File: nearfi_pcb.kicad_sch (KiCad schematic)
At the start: 45 parts, among them J1 PWR_CNN, J2 PROG_CNN, Q1 MMBT3904, SW1 SRST_BTN, U2 TLV1117-33, U3 AT24CS02-STUM, U4 TPL5010, U5 ESP32-S3-MINI-1

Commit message: finished rev D
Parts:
- D1, D4: LCSC C2976072 -> C965555
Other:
- note added: "C5 and C6 should be tantalum capacitors"
- note removed: "Note: - C5 and C6 should be tantalum capacitors"
- moved on the sheet: D8, D9
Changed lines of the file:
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@@
     (stroke (width 0) (type default) (color 0 0 0 0))
   )
-  (wire (pts (xy 173.99 100.33) (xy 173.99 101.6))
+  (wire (pts (xy 173.99 97.79) (xy 173.99 99.06))
     (stroke (width 0) (type default) (color 0 0 0 0))
   )
@@
     (stroke (width 0) (type default) (color 0 0 0 0))
   )
+  (wire (pts (xy 173.99 85.09) (xy 173.99 90.17))
+    (stroke (width 0) (type default) (color 0 0 0 0))
+  )
   (polyline (pts (xy 13.97 121.92) (xy 13.97 161.29))
     (stroke (width 0) (type default) (color 0 0 0 0))
@@
     (stroke (width 0) (type default) (color 0 0 0 0))
   )
-  (wire (pts (xy 167.64 82.55) (xy 167.64 86.36))
-    (stroke (width 0) (type default) (color 0 0 0 0))
-  )
   (wire (pts (xy 20.32 149.86) (xy 20.32 151.13))
     (stroke (width 0) (type default) (color 0 0 0 0))
@@
     (stroke (width 0) (type default) (color 0 0 0 0))
   )
-  (wire (pts (xy 167.64 93.98) (xy 167.64 95.25))
+  (wire (pts (xy 167.64 97.79) (xy 167.64 99.06))
     (stroke (width 0) (type default) (color 0 0 0 0))
   )
@@
     (stroke (width 0) (type dash) (color 0 0 0 0))
   )
+  (wire (pts (xy 167.64 82.55) (xy 167.64 90.17))
+    (stroke (width 0) (type default) (color 0 0 0 0))
+  )
   (wire (pts (xy 152.4 138.43) (xy 152.4 139.7))
     (stroke (width 0) (type default) (color 0 0 0 0))
@@
   )
   (wire (pts (xy 151.13 90.17) (xy 162.56 90.17))
-    (stroke (width 0) (type default) (color 0 0 0 0))
-  )
-  (wire (pts (xy 173.99 85.09) (xy 173.99 92.71))
     (stroke (width 0) (type default) (color 0 0 0 0))
   )
@@
     (effects (font (size 2 2)) (justify left bottom))
   )
-  (text "Note: \n- C5 and C6 should be tantalum capacitors" (at 194.31 62.23 0)
+  (text "C5 and C6 should be\ntantalum capacitors" (at 200.66 59.69 0)
     (effects (font (size 1.27 1.27)) (justify left bottom))
   )
@@
     (pin "1")
   )
-  (symbol (lib_id "power:GND") (at 167.64 95.25 0) (unit 1)
-    (in_bom yes) (on_board yes)
-    (property "Reference" "#PWR0130" (id 0) (at 167.64 101.6 0)
-      (effects (font (size 1.27 1.27)) hide)
-    )
-    (property "Value" "GND" (id 1) (at 167.64 99.06 0))
-    (property "Footprint" "" (id 2) (at 167.64 95.25 0)
-      (effects (font (size 1.27 1.27)) hide)
-    )
-    (property "Datasheet" "" (id 3) (at 167.64 95.25 0)
+  (symbol (lib_id "power:GND") (at 167.64 99.06 0) (unit 1)
+    (in_bom yes) (on_board yes)
+    (property "Reference" "#PWR0130" (id 0) (at 167.64 105.41 0)
+      (effects (font (size 1.27 1.27)) hide)
+    )
+    (property "Value" "GND" (id 1) (at 167.64 102.87 0))
+    (property "Footprint" "" (id 2) (at 167.64 99.06 0)
+      (effects (font (size 1.27 1.27)) hide)
+    )
+    (property "Datasheet" "" (id 3) (at 167.64 99.06 0)
       (effects (font (size 1.27 1.27)) hide)
     )
@@
     (pin "1")
   )
-  (symbol (lib_id "Diode:ESD9B5.0ST5G") (at 167.64 90.17 270) (unit 1)
-    (in_bom yes) (on_board yes)
-    (property "Reference" "D8" (id 0) (at 170.18 88.8999 90)
-      (effects (font (size 1.27 1.27)) (justify left))
-    )
-    (property "Value" "ESD9B5.0ST5G" (id 1) (at 170.18 91.44 90)
-      (effects (font (size 1.27 1.27)) (justify left))
-    )
-    (property "Footprint" "Diode_SMD:D_SOD-923" (id 2) (at 167.64 90.17 0)
-      (effects (font (size 1.27 1.27)) hide)
-    )
-    (property "Datasheet" "https://www.onsemi.com/pub/Collateral/ESD9B-D.PDF" (id 3) (at 167.64 90.17 0)
-      (effects (font (size 1.27 1.27)) hide)
-    )
-    (property "Check" "y" (id 4) (at 167.64 90.17 0)
-      (effects (font (size 1.27 1.27)) hide)
-    )
-    (property "LCSC" "C111566" (id 5) (at 167.64 90.17 0)
+  (symbol (lib_id "Diode:ESD9B5.0ST5G") (at 167.64 93.98 90) (mirror x) (unit 1)
+    (in_bom yes) (on_board yes)
+    (property "Reference" "D8" (id 0) (at 165.1 92.7099 90)
+      (effects (font (size 1.27 1.27)) (justify left))
+    )
+    (property "Value" "ESD9B5.0ST5G" (id 1) (at 165.1 95.25 90)
+      (effects (font (size 1.27 1.27)) (justify left))
+    )
+    (property "Footprint" "Diode_SMD:D_SOD-923" (id 2) (at 167.64 93.98 0)
+      (effects (font (size 1.27 1.27)) hide)
+    )
+    (property "Datasheet" "https://www.onsemi.com/pub/Collateral/ESD9B-D.PDF" (id 3) (at 167.64 93.98 0)
+      (effects (font (size 1.27 1.27)) hide)
+    )
+    (property "Check" "y" (id 4) (at 167.64 93.98 0)
+      (effects (font (size 1.27 1.27)) hide)
+    )
+    (property "LCSC" "C111566" (id 5) (at 167.64 93.98 0)
       (effects (font (size 1.27 1.27)) hide)
     )
@@
     (pin "1")
   )
-  (symbol (lib_id "Diode:ESD9B5.0ST5G") (at 173.99 96.52 90) (unit 1)
-    (in_bom yes) (on_board yes)
-    (property "Reference" "D9" (id 0) (at 176.53 95.2499 90)
+  (symbol (lib_id "Diode:ESD9B5.0ST5G") (at 173.99 93.98 90) (unit 1)
+    (in_bom yes) (on_board yes)
+    (property "Reference" "D9" (id 0) (at 176.53 92.7099 90)
       (effects (font (size 1.27 1.27)) (justify right))
     )
-    (property "Value" "ESD9B5.0ST5G" (id 1) (at 176.53 97.79 90)
+    (property "Value" "ESD9B5.0ST5G" (id 1) (at 176.53 95.25 90)
       (effects (font (size 1.27 1.27)) (justify right))
     )
-    (property "Footprint" "Diode_SMD:D_SOD-923" (id 2) (at 173.99 96.52 0)
-      (effects (font (size 1.27 1.27)) hide)
-    )
-    (property "Datasheet" "https://www.onsemi.com/pub/Collateral/ESD9B-D.PDF" (id 3) (at 173.99 96.52 0)
-      (effects (font (size 1.27 1.27)) hide)
-    )
-    (property "Check" "y" (id 4) (at 173.99 96.52 0)
-      (effects (font (size 1.27 1.27)) hide)
-    )
-    (property "LCSC" "C111566" (id 5) (at 173.99 96.52 0)
+    (property "Footprint" "Diode_SMD:D_SOD-923" (id 2) (at 173.99 93.98 0)
+      (effects (font (size 1.27 1.27)) hide)
+    )
+    (property "Datasheet" "https://www.onsemi.com/pub/Collateral/ESD9B-D.PDF" (id 3) (at 173.99 93.98 0)
+      (effects (font (size 1.27 1.27)) hide)
+    )
+    (property "Check" "y" (id 4) (at 173.99 93.98 0)
+      (effects (font (size 1.27 1.27)) hide)
+    )
+    (property "LCSC" "C111566" (id 5) (at 173.99 93.98 0)
       (effects (font (size 1.27 1.27)) hide)
     )
@@
     (pin "2")
   )
-  (symbol (lib_id "power:GND") (at 173.99 101.6 0) (unit 1)
-    (in_bom yes) (on_board yes)
-    (property "Reference" "#PWR0129" (id 0) (at 173.99 107.95 0)
-      (effects (font (size 1.27 1.27)) hide)
-    )
-    (property "Value" "GND" (id 1) (at 173.99 105.41 0))
-    (property "Footprint" "" (id 2) (at 173.99 101.6 0)
-      (effects (font (size 1.27 1.27)) hide)
-    )
-    (property "Datasheet" "" (id 3) (at 173.99 101.6 0)
+  (symbol (lib_id "power:GND") (at 173.99 99.06 0) (unit 1)
+    (in_bom yes) (on_board yes)
+    (property "Reference" "#PWR0129" (id 0) (at 173.99 105.41 0)
+      (effects (font (size 1.27 1.27)) hide)
+    )
+    (property "Value" "GND" (id 1) (at 173.99 102.87 0))
+    (property "Footprint" "" (id 2) (at 173.99 99.06 0)
+      (effects (font (size 1.27 1.27)) hide)
+    )
+    (property "Datasheet" "" (id 3) (at 173.99 99.06 0)
       (effects (font (size 1.27 1.27)) hide)
     )
@@
       (effects (font (size 1.27 1.27)) (justify left top) hide)
     )
-    (property "Datasheet" "https://www.mouser.com/pdfDocs/WS2812B-2020_V10_EN_181106150240761.pdf" (id 3) (at 267.97 48.895 0)
+    (property "Datasheet" "https://datasheet.lcsc.com/lcsc/2012110135_Worldsemi-WS2812B-2020_C965555.pdf" (id 3) (at 267.97 48.895 0)
       (effects (font (size 1.27 1.27)) (justify left top) hide)
     )
-    (property "LCSC" "C2976072" (id 4) (at 265.43 39.37 0)
+    (property "LCSC" "C965555" (id 4) (at 265.43 39.37 0)
       (effects (font (size 1.27 1.27)) hide)
     )
@@
       (effects (font (size 1.27 1.27)) (justify left top) hide)
     )
-    (property "Datasheet" "https://www.mouser.com/pdfDocs/WS2812B-2020_V10_EN_181106150240761.pdf" (id 3) (at 267.97 81.915 0)
+    (property "Datasheet" "https://datasheet.lcsc.com/lcsc/2012110135_Worldsemi-WS2812B-2020_C965555.pdf" (id 3) (at 267.97 81.915 0)
       (effects (font (size 1.27 1.27)) (justify left top) hide)
     )
-    (property "LCSC" "C2976072" (id 4) (at 265.43 72.39 0)
-      (effects (font (size 1.27 1.27)) hide)
-    )
+    (property "LCSC" "C965555" (id 4) (at 265.43 72.39 0)
+      (effects (font (size 1.27 1.27)) hide)
+    )

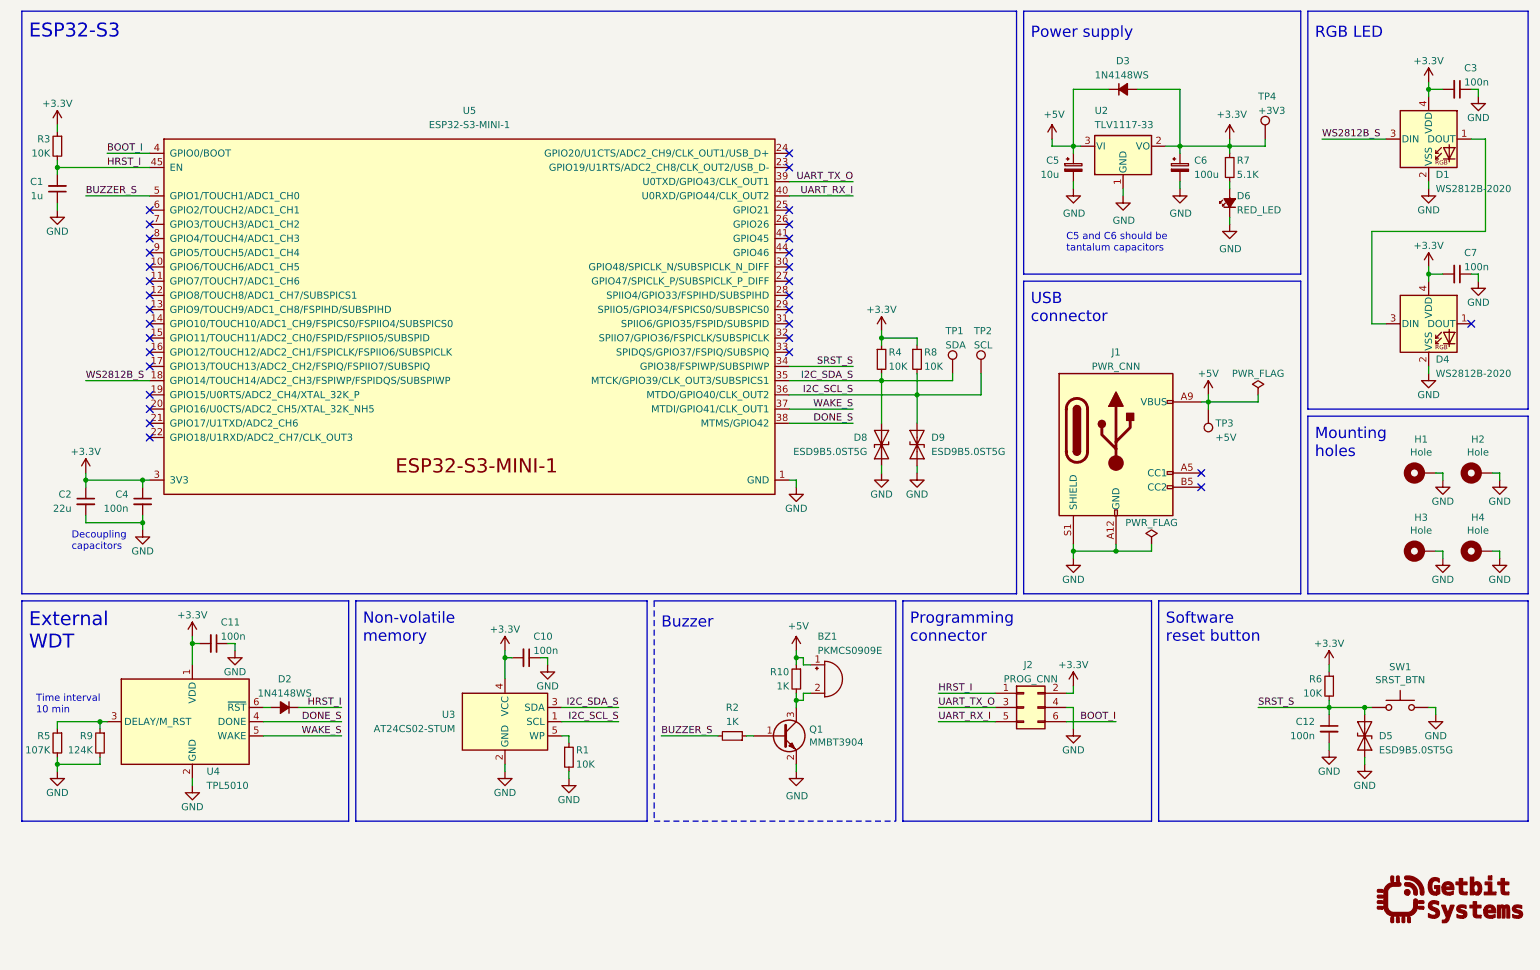
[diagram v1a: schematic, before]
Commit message: updated to work with kicad v8
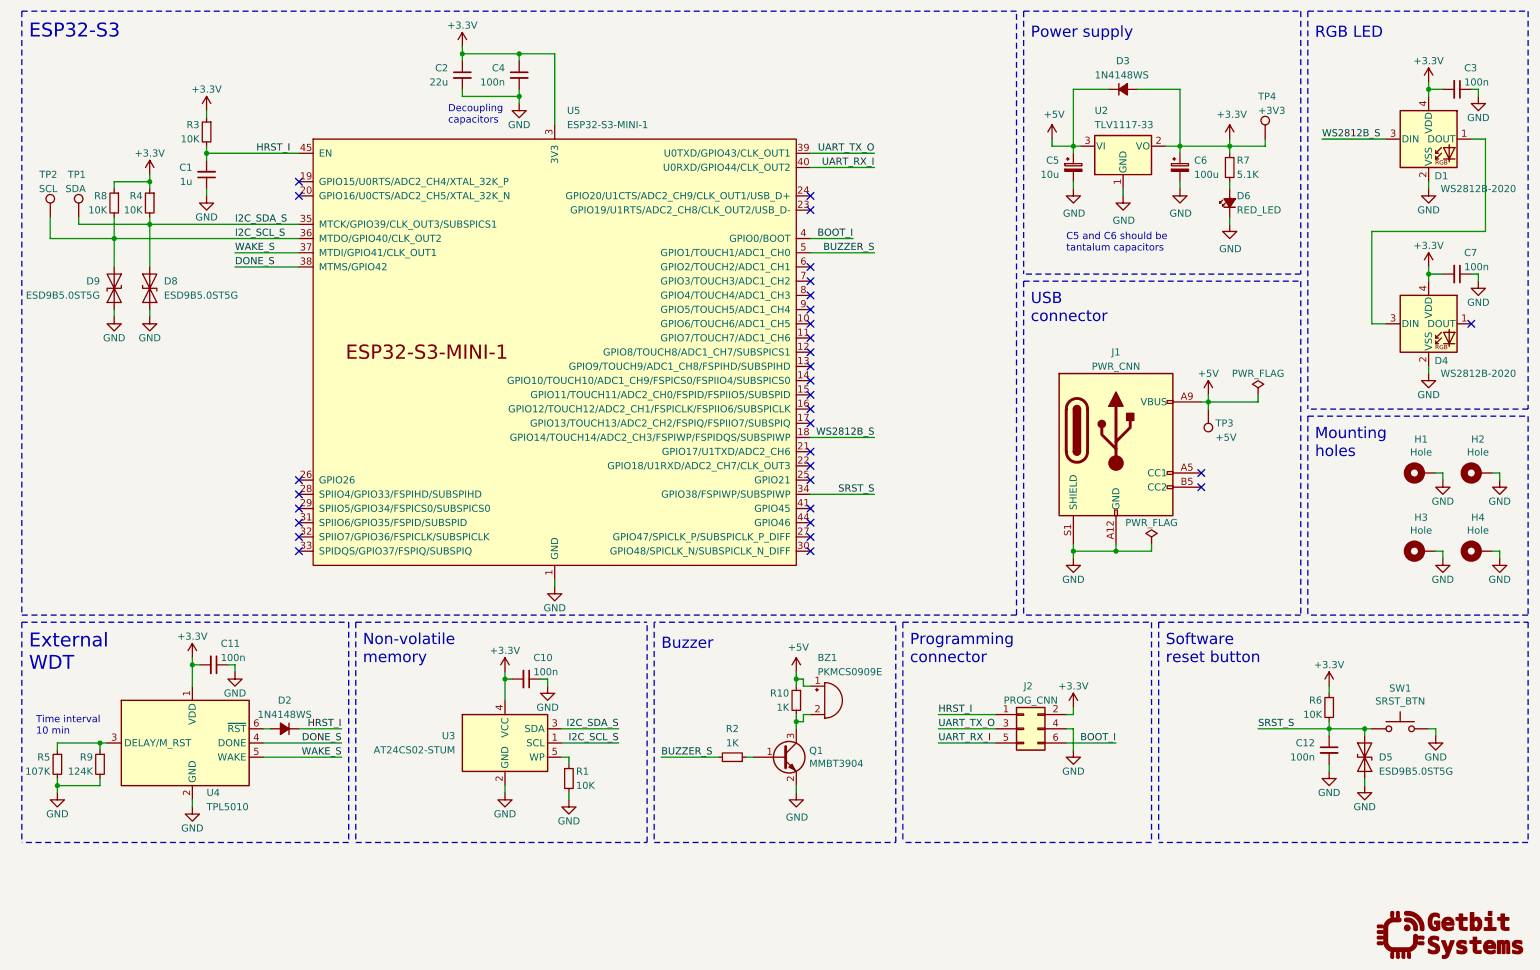
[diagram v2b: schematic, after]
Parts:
- removed D1, D4: WS2812B-2020, Misc:WS2812B-2020, symbol Misc:WS2812B-2020
- removed U5: ESP32-S3-MINI-1, Espressif:ESP32-S3-MINI-1, symbol Espressif:ESP32-S3-MINI-1
- added D1, D4: WS2812B-2020, LED_SMD:LED_WS2812B-2020_PLCC4_2.0x2.0mm, symbol LED:WS2812B-2020
- added U5: ESP32-S3-MINI-1, PCM_Espressif:ESP32-S3-MINI-1, symbol PCM_Espressif:ESP32-S3-MINI-1
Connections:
- net +3.3V: now also D1.4 (VDD), D4.4 (VDD), U5.3 (3V3)
- net BOOT_I: now also U5.4 (GPIO0/BOOT)
- net BUZZER_S: now also U5.5 (GPIO1/TOUCH1/ADC1_CH0)
- net DONE_S: now also U5.38 (MTMS/GPIO42)
- net GND: now also D1.2 (VSS), D4.2 (VSS), U5.1 (GND), U5.2 (GND), U5.42 (GND), U5.43 (GND), U5.46 (GND), U5.47 (GND), U5.48 (GND), U5.49 (GND), U5.50 (GND), U5.51 (GND), U5.52 (GND), U5.53 (GND), U5.54 (GND), U5.55 (GND), U5.56 (GND), U5.57 (GND), U5.58 (GND), U5.59 (GND), U5.60 (GND), U5.61 (GND), U5.62 (GND), U5.63 (GND), U5.64 (GND), U5.65 (GND)
- net HRST_I: now also U5.45 (EN)
- net I2C_SCL_S: now also U5.36 (MTDO/GPIO40/CLK_OUT2)
- net I2C_SDA_S: now also U5.35 (MTCK/GPIO39/CLK_OUT3/SUBSPICS1)
- net SRST_S: now also U5.34 (GPIO38/FSPIWP/SUBSPIWP)
- net UART_RX_I: now also U5.40 (U0RXD/GPIO44/CLK_OUT2)
- net UART_TX_O: now also U5.39 (U0TXD/GPIO43/CLK_OUT1)
- net WAKE_S: now also U5.37 (MTDI/GPIO41/CLK_OUT1)
- net WS2812B_S: now also D1.3 (DIN), U5.18 (GPIO14/TOUCH14/ADC2_CH3/FSPIWP/FSPIDQS/SUBSPIWP)
- new net: D1.1 (DOUT), D4.3 (DIN)
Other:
- moved on the sheet: BZ1, C1, C10, C11, C12, C2, C4, D2, D5, D8, D9, J2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

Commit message: updated schematic and layout
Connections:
- net GND: no longer U5.1 (GND), U5.2 (GND), U5.42 (GND), U5.43 (GND), U5.46 (GND), U5.47 (GND), U5.48 (GND), U5.49 (GND), U5.50 (GND), U5.51 (GND), U5.52 (GND), U5.53 (GND), U5.54 (GND), U5.55 (GND), U5.56 (GND), U5.57 (GND), U5.58 (GND), U5.59 (GND), U5.60 (GND), U5.61 (GND), U5.62 (GND), U5.63 (GND), U5.64 (GND), U5.65 (GND)
- new net: U5.1 (GND), U5.2 (GND), U5.42 (GND), U5.43 (GND), U5.46 (GND), U5.47 (GND), U5.48 (GND), U5.49 (GND), U5.50 (GND), U5.51 (GND), U5.52 (GND), U5.53 (GND), U5.54 (GND), U5.55 (GND), U5.56 (GND), U5.57 (GND), U5.58 (GND), U5.59 (GND), U5.60 (GND), U5.61 (GND), U5.62 (GND), U5.63 (GND), U5.64 (GND), U5.65 (GND)
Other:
- moved on the sheet: C1, C2, C4, D8, D9, R3, R4, R8, TP1, TP2, U5
